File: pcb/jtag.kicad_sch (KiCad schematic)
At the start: 37 parts

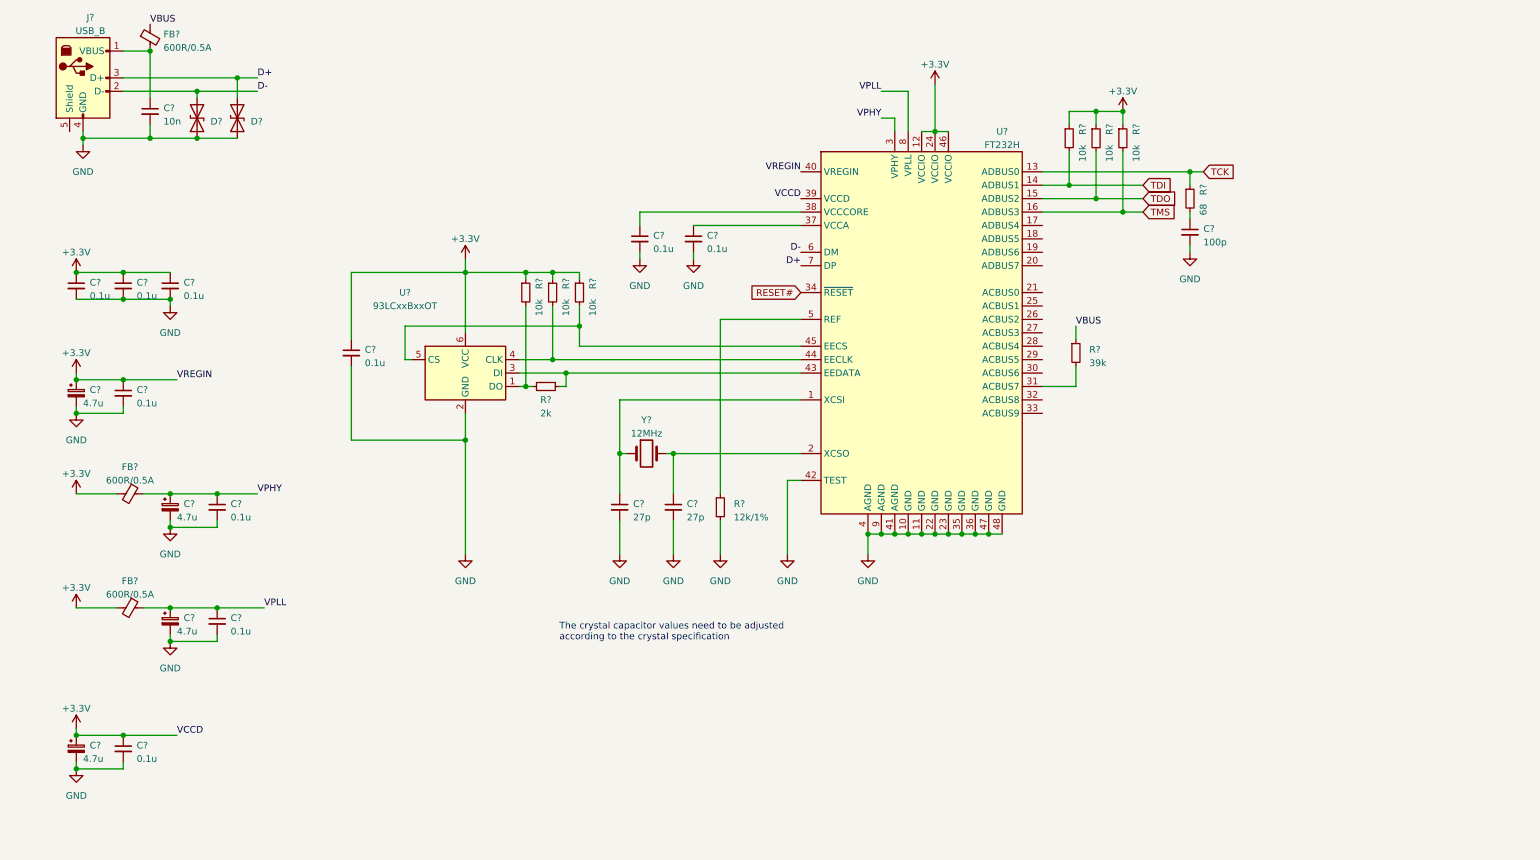
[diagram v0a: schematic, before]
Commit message: add buffer to jtag interface
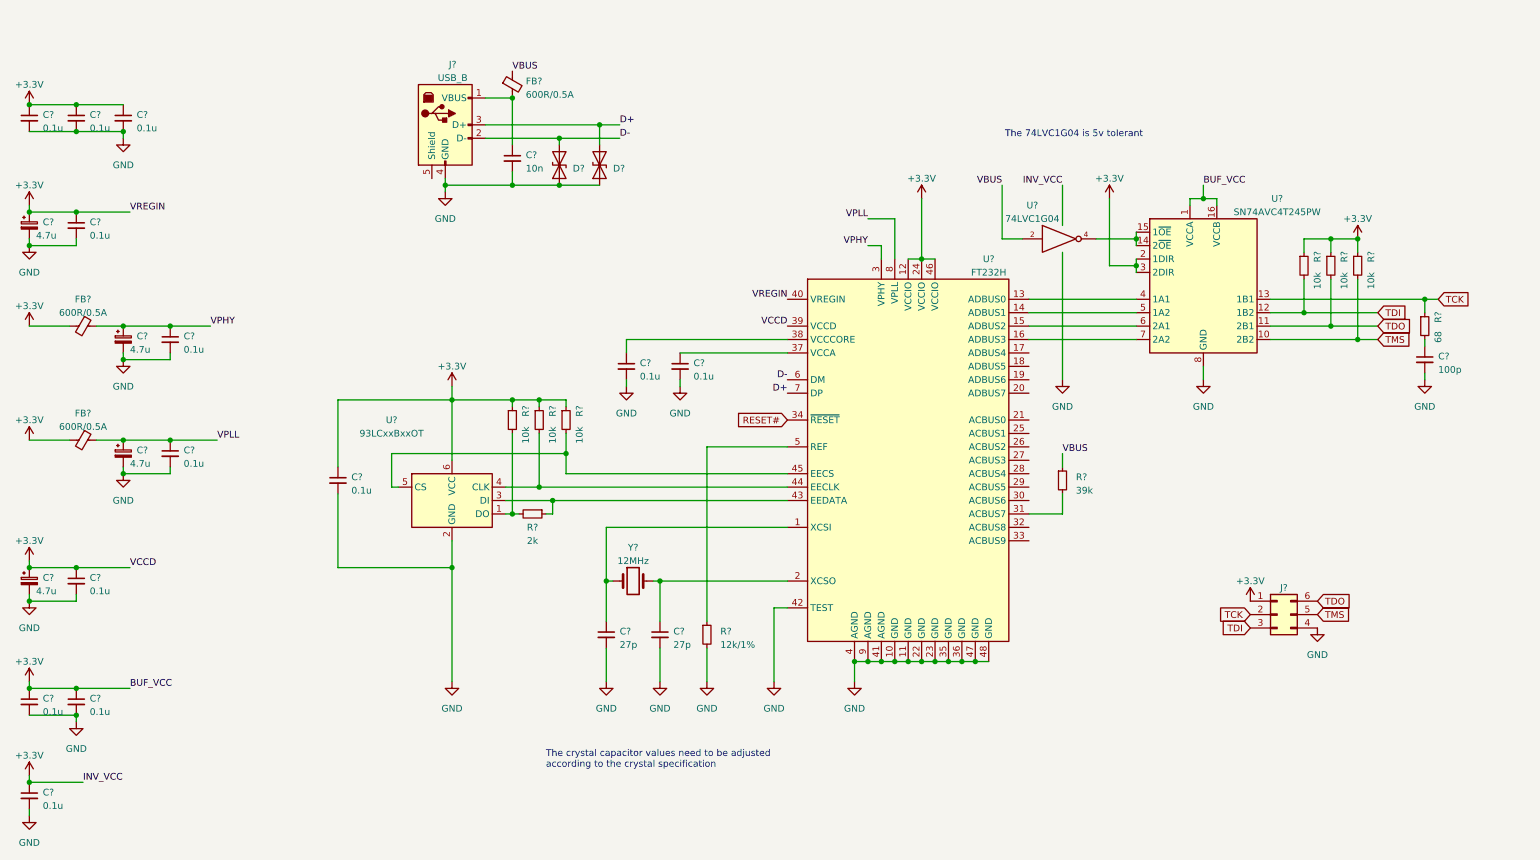
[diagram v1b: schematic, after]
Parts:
- added C? (x3): 0.1u, symbol Device:C_Small
- added J?: Conn_02x03_Counter_Clockwise, symbol Connector_Generic:Conn_02x03_Counter_Clockwise
- added U?: SN74AVC4T245PW, Package_SO:TSSOP-16_4.4x5mm_P0.65mm, symbol Logic_LevelTranslator:SN74AVC4T245PW
- added U?: 74LVC1G04, symbol 74xGxx:74LVC1G04
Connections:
- net +3V3: now also C?.1, C?.1, C?.1, J?.1 (Pin_1), U?.1 (VCCA), U?.16 (VCCB), U?.2 (1DIR), U?.3 (2DIR), U?.5 (VCC)
- net GND: now also C?.2, C?.2, C?.2, J?.4 (Pin_4), U?.3 (GND), U?.8 (GND), U?.9 (GND)
- net TCK: now also J?.2 (Pin_2), U?.13 (1B1); no longer U?.13 (ADBUS0)
- net TDI: now also J?.3 (Pin_3), U?.12 (1B2); no longer U?.14 (ADBUS1)
- net TDO: now also J?.6 (Pin_6), U?.11 (2B1); no longer U?.15 (ADBUS2)
- net TMS: now also J?.5 (Pin_5), U?.10 (2B2); no longer U?.16 (ADBUS3)
- net VBUS: now also U?.2
- new net: U?.13 (ADBUS0), U?.4 (1A1)
- new net: U?.14 (ADBUS1), U?.5 (1A2)
- new net: U?.15 (ADBUS2), U?.6 (2A1)
- new net: U?.16 (ADBUS3), U?.7 (2A2)
- new net: U?.14 (2~OE), U?.15 (1~OE), U?.4
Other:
- note added: "The 74LVC1G04 is 5v tolerant"
- title: (none) -> JTAG interface
- moved on the sheet: C?, D?, FB?, J?, R?, U?, Y?

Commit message: add power supply
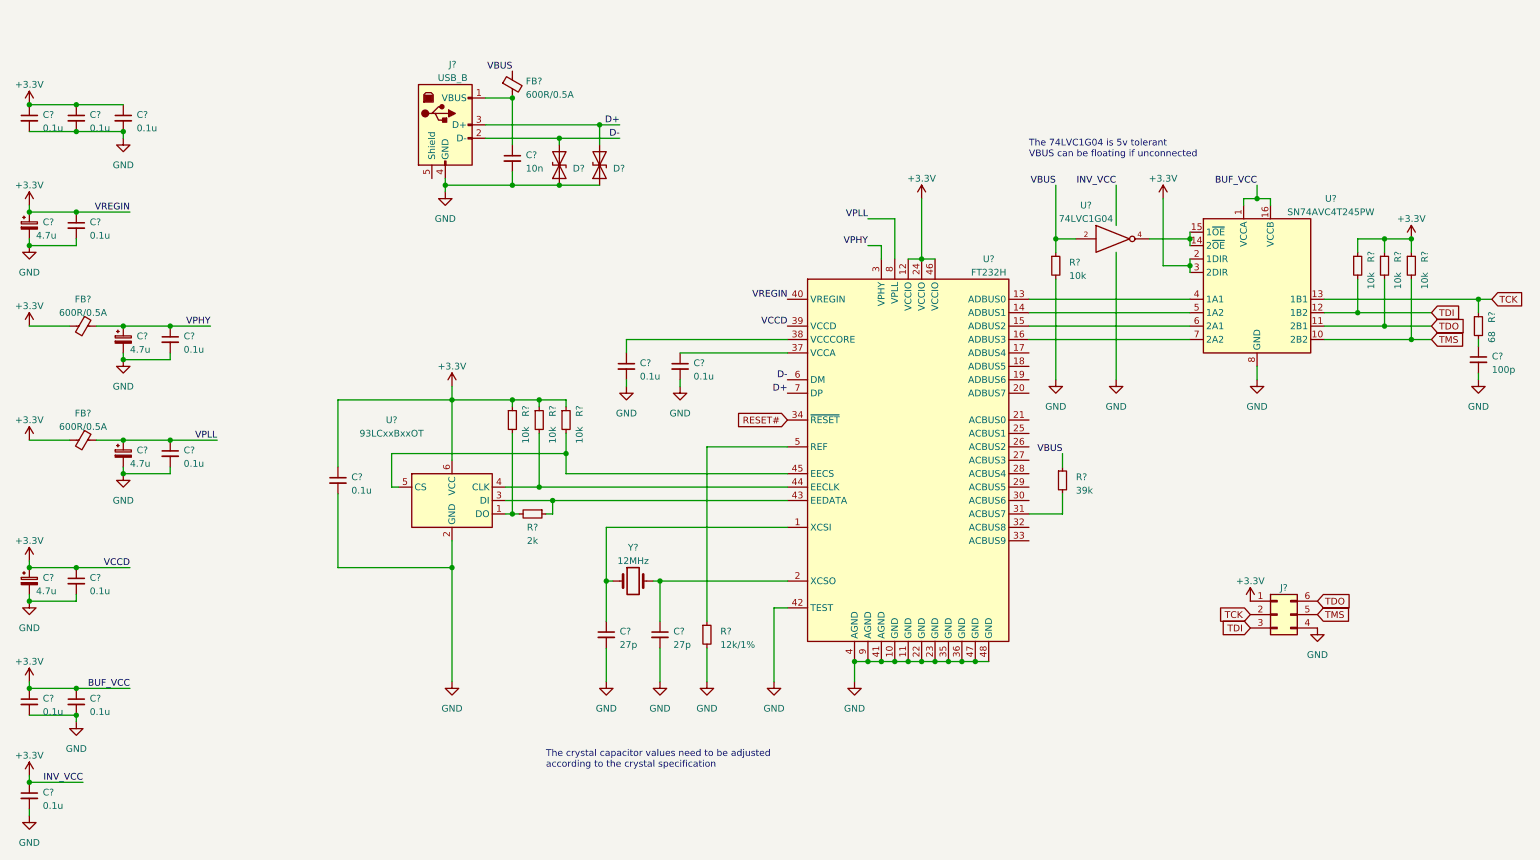
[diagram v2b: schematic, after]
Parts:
- added R?: 10k, symbol Device:R_Small
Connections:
- net GND: now also R?.2
- net VBUS: now also R?.1
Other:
- note added: "The 74LVC1G04 is 5v tolerant VBUS can be floating if unconnected"
- note removed: "The 74LVC1G04 is 5v tolerant"
- moved on the sheet: C?, R?, U?

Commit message: add the usb to spi interface
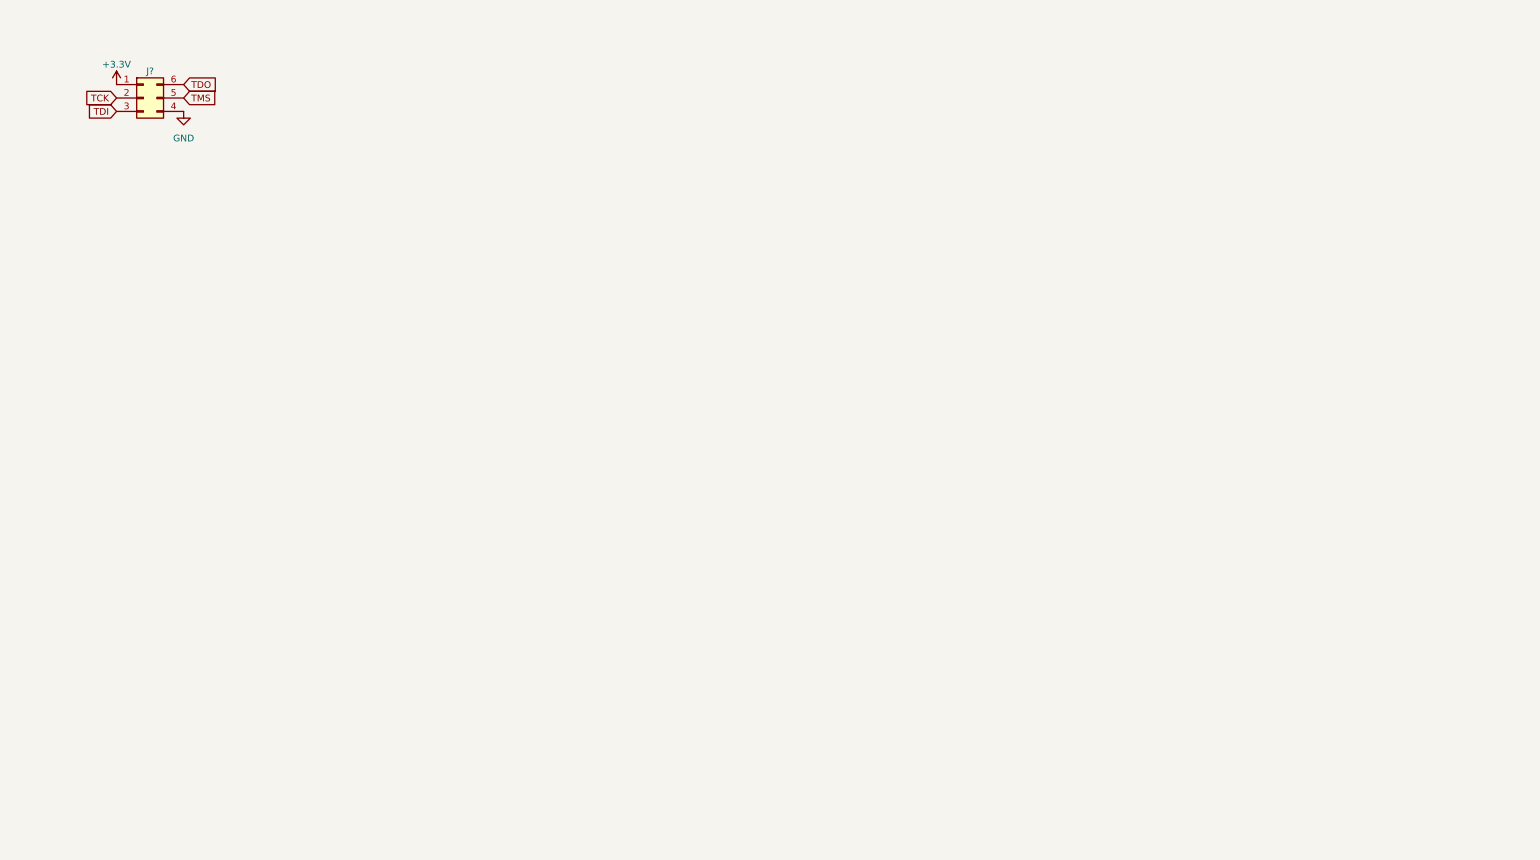
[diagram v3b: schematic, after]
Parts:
- removed C? (x2): 27p, symbol Device:C_Small
- removed C? (x13): 0.1u, symbol Device:C_Small
- removed C?: 100p, symbol Device:C_Small
- removed C? (x4): 4.7u, symbol Device:C_Polarized_Small
- removed C?: 10n, symbol Device:C_Small
- removed D? (x2): D_TVS, symbol Device:D_TVS
- removed FB? (x3): 600R/0.5A, symbol Device:FerriteBead_Small
- removed J?: USB_B, symbol Connector:USB_B
- removed J?: Conn_02x03_Counter_Clockwise, symbol Connector_Generic:Conn_02x03_Counter_Clockwise
- removed R?: 2k, symbol Device:R_Small
- removed R?: 12k/1%, symbol Device:R_Small
- removed R? (x7): 10k, symbol Device:R_Small
- removed R?: 68, symbol Device:R_Small
- removed R?: 39k, symbol Device:R_Small
- removed U?: FT232H, symbol Interface_USB:FT232H
- removed U?: SN74AVC4T245PW, Package_SO:TSSOP-16_4.4x5mm_P0.65mm, symbol Logic_LevelTranslator:SN74AVC4T245PW
- removed U?: 74LVC1G04, symbol 74xGxx:74LVC1G04
- removed U?: 93LCxxBxxOT, Package_TO_SOT_SMD:SOT-23-6, symbol Memory_EEPROM:93LCxxBxxOT
- removed Y?: 12MHz, symbol Device:Crystal
- added J?: Conn_02x03_Counter_Clockwise, symbol Connector_Generic:Conn_02x03_Counter_Clockwise
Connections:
- net +3V3: now also J?.1 (Pin_1)
- net GND: now also J?.4 (Pin_4)
- net TCK: now also J?.2 (Pin_2)
- net TDI: now also J?.3 (Pin_3)
- net TDO: now also J?.6 (Pin_6)
- net TMS: now also J?.5 (Pin_5)
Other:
- note removed: "The 74LVC1G04 is 5v tolerant VBUS can be floating if unconnected"
- note removed: "The crystal capacitor values need to be adjusted according to the crystal specification"
- title: JTAG interface -> (none)
